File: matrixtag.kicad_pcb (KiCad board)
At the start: 2 copper layers, 57 x 32 mm, 24 parts, among them P1 ISP, Q1 2N7002, Q2 2N7002, Q3 2N7002, Q4 2N7002, Q5 2N7002, Q6 2N7002, Q7 2N7002, Q8 2N7002, SW1 RESET, U1 ATTINY4313-S

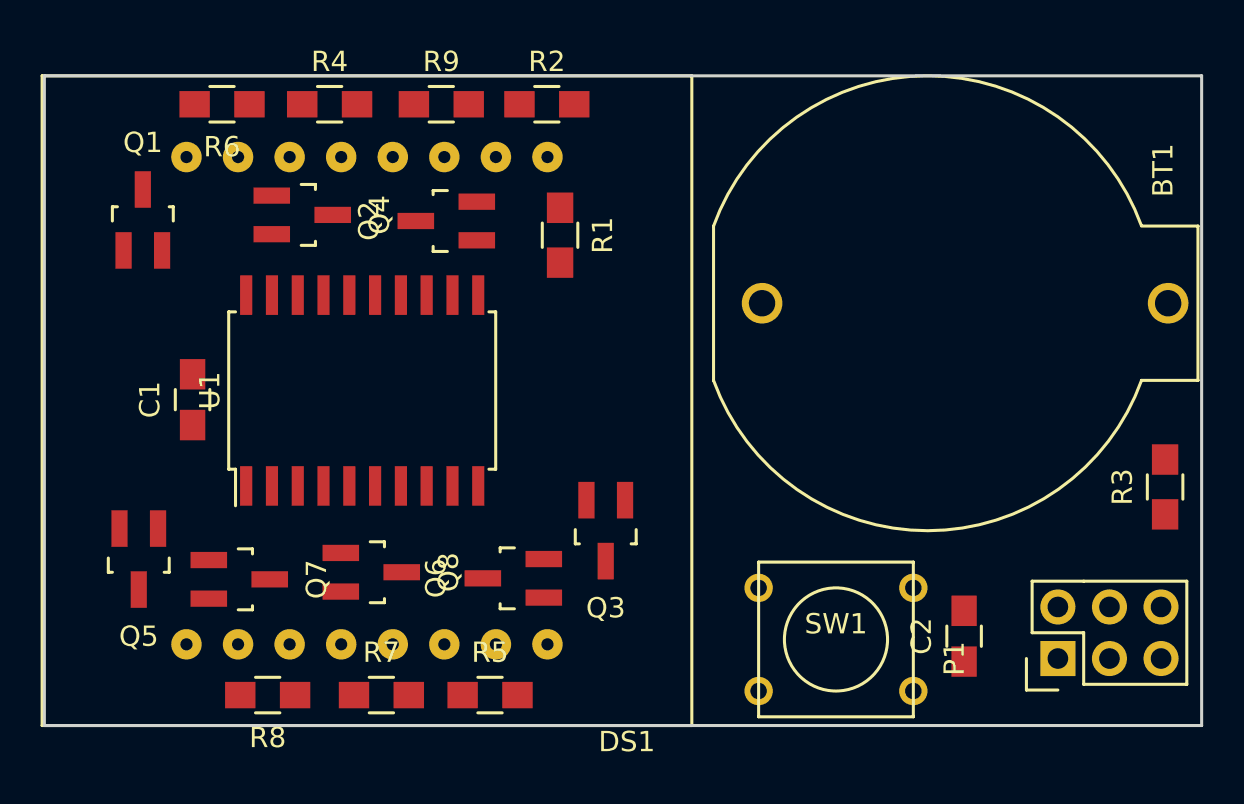
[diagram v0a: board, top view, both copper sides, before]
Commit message: Moved parts to front layer
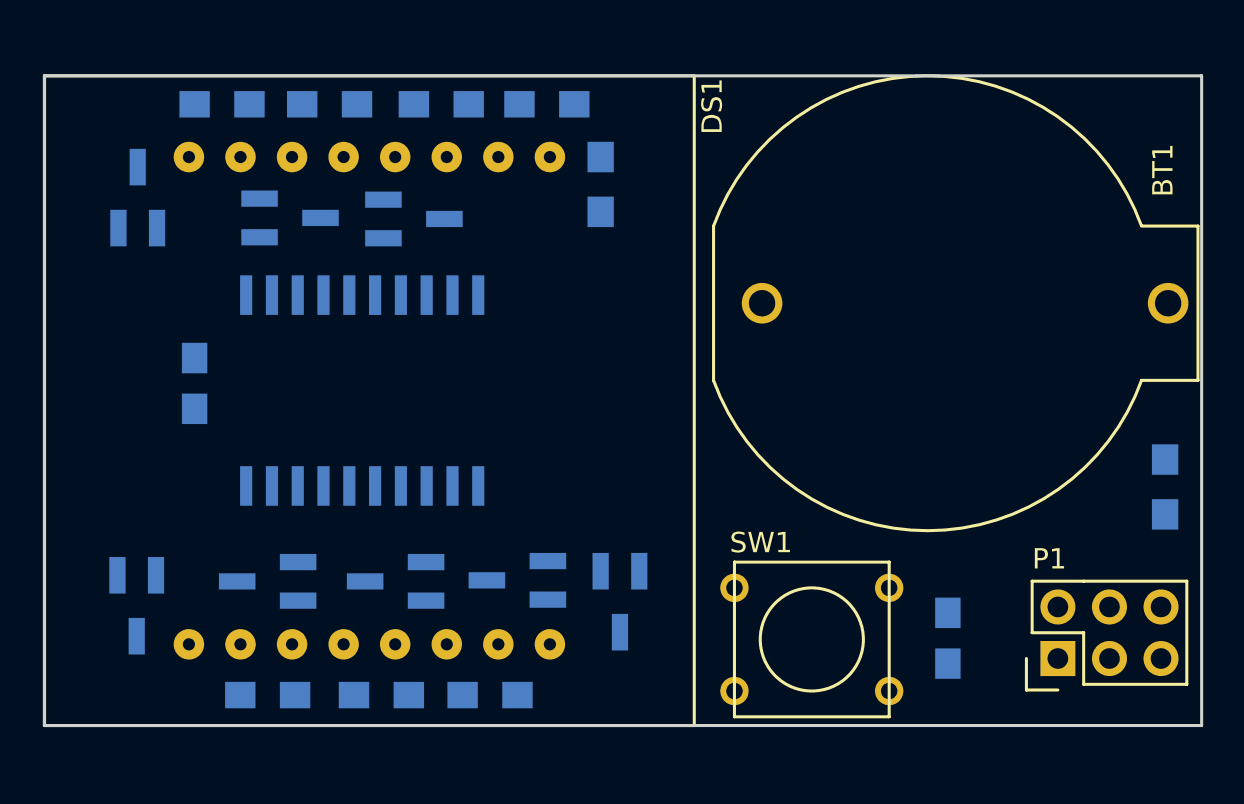
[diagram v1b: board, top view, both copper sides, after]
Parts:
- C1, C2, Q1, Q2, Q3, Q4, Q5, Q6, Q7, Q8, R1, R2, R3, R4, R5, R6, R7, R8, R9, U1: moved to B.Cu
- moved Q3 3.57 mm to (196.3, 112.9), turned to 0 degrees
- moved R1 3.20 mm to (195.4, 92.3)
- moved Q5 2.30 mm to (172.6, 113.1), turned to 0 degrees
- moved Q2 1.60 mm to (186.2, 94.0)
- moved Q7 1.40 mm to (179.0, 111.9)
- moved Q8 1.28 mm to (185.3, 111.9)
- moved SW1 1.19 mm to (205.8, 114.8)
- moved Q1 1.13 mm to (172.6, 93.0), turned to 180 degrees
- moved C2 0.81 mm to (212.5, 114.7), turned to 270 degrees
- moved C1 0.81 mm to (175.4, 102.2), turned to 270 degrees
- moved Q4 0.62 mm to (180.1, 94.0), turned to 90 degrees
- moved Q6 0.22 mm to (191.3, 111.8), turned to 270 degrees
- moved DS1 0.12 mm to (184.0, 103.0)
- turned R3 to 270 degrees
- turned U1 to 270 degrees

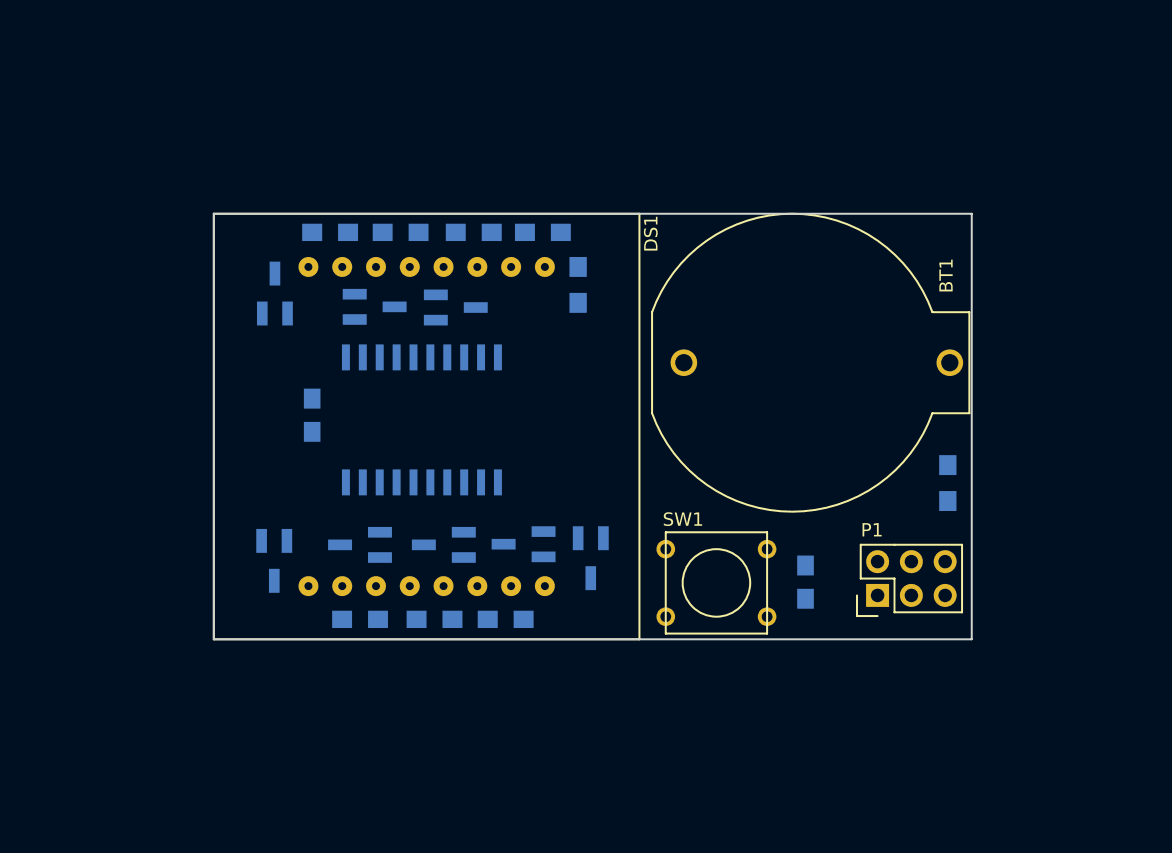
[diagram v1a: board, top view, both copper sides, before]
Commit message: Finished matrix tag schematic and layout
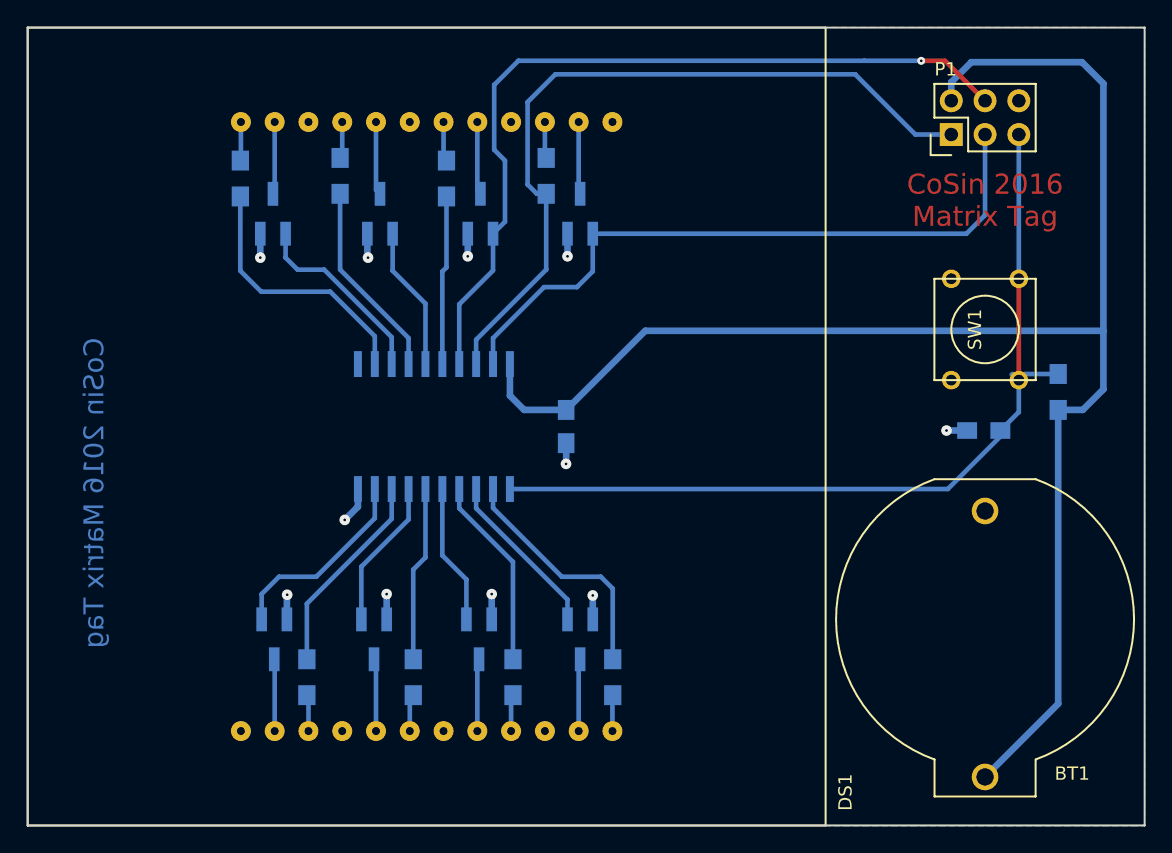
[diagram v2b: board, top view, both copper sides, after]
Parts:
- DS1: value LDM-1088AX -> CSM-88261EG; footprint nametag:LDM-1088 -> nametag:CSM-88261
- moved P1 35.1 mm to (223.5, 81.0)
- moved R7 34.1 mm to (177.5, 84.2), turned to 270 degrees
- moved R8 33.8 mm to (185.5, 84.3), turned to 270 degrees
- moved R2 33.5 mm to (190.5, 121.8), turned to 90 degrees
- moved R4 33.5 mm to (183.0, 121.8), turned to 90 degrees
- moved Q3 30.4 mm to (180.5, 87.0), turned to 180 degrees
- moved R1 29.6 mm to (198.0, 121.8), turned to 90 degrees
- moved SW1 27.8 mm to (226.0, 95.7), turned to 90 degrees
- moved BT1 24.1 mm to (226.0, 117.5), turned to 270 degrees
- moved Q1 23.7 mm to (195.6, 87.0)
- moved C1 19.1 mm to (194.5, 103.0), turned to 90 degrees
- moved C2 17.6 mm to (225.9, 103.3), turned to 180 degrees
- moved R5 15.6 mm to (175.0, 121.8), turned to 90 degrees
- moved Q6 13.3 mm to (180.1, 119.0), turned to 0 degrees
- moved Q8 12.5 mm to (195.6, 119.0), turned to 0 degrees
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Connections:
- DS1 pad 1: Net-(DS1-Pad1) -> (no net)
- DS1 pad 10: Net-(DS1-Pad10) -> (no net)
- DS1 pad 15: Net-(DS1-Pad15) -> (no net)
- DS1 pad 4: Net-(DS1-Pad4) -> (no net)
- DS1 pad 7: Net-(DS1-Pad7) -> (no net)
- P1 pad 1: /COL7 -> /MISO
- P1 pad 2: (no net) -> VCC
- P1 pad 3: /COL8 -> /COL1
- P1 pad 4: /COL6 -> /COL2
- Q1 pad 1: /ROW1 -> /COL1
- Q1 pad 3: Net-(DS1-Pad9) -> Net-(DS1-Pad23)
- Q2 pad 1: /ROW2 -> /COL2
- Q2 pad 3: Net-(DS1-Pad14) -> Net-(DS1-Pad20)
- Q3 pad 1: /ROW3 -> /COL3
- Q3 pad 3: Net-(DS1-Pad8) -> Net-(DS1-Pad17)
- Q4 pad 1: /ROW4 -> /COL4
- Q4 pad 3: Net-(DS1-Pad12) -> Net-(DS1-Pad14)
- Q5 pad 1: /ROW5 -> /COL5
- Q5 pad 3: Net-(DS1-Pad1) -> Net-(DS1-Pad2)
- Q6 pad 1: /ROW6 -> /COL6
- Q6 pad 3: Net-(DS1-Pad7) -> Net-(DS1-Pad5)
- Q7 pad 1: /ROW7 -> /COL7
- Q7 pad 3: Net-(DS1-Pad2) -> Net-(DS1-Pad8)
- Q8 pad 1: /ROW8 -> /COL8
- Q8 pad 3: Net-(DS1-Pad5) -> Net-(DS1-Pad11)
- R1 pad 1: Net-(DS1-Pad16) -> Net-(DS1-Pad12)
- R1 pad 2: /COL8 -> /ROW8
- R2 pad 1: Net-(DS1-Pad15) -> Net-(DS1-Pad9)
- R2 pad 2: /COL7 -> /ROW7
- R4 pad 1: Net-(DS1-Pad11) -> Net-(DS1-Pad6)
- R4 pad 2: /COL6 -> /ROW6
- R5 pad 1: Net-(DS1-Pad6) -> Net-(DS1-Pad3)
- R5 pad 2: /COL5 -> /ROW5
- R6 pad 1: Net-(DS1-Pad10) -> Net-(DS1-Pad13)
- R6 pad 2: /COL4 -> /ROW4
- R7 pad 1: Net-(DS1-Pad4) -> Net-(DS1-Pad16)
- R7 pad 2: /COL3 -> /ROW3
- R8 pad 1: Net-(DS1-Pad3) -> Net-(DS1-Pad19)
- R8 pad 2: /COL2 -> /ROW2
- R9 pad 1: Net-(DS1-Pad13) -> Net-(DS1-Pad22)
- R9 pad 2: /COL1 -> /MISO
- U1 pad 11: /ROW7 -> (no net)
- U1 pad 12: /COL1 -> /ROW4
- U1 pad 13: /COL2 -> /COL4
- U1 pad 14: /COL3 -> /ROW3
- U1 pad 15: /COL4 -> /COL3
- U1 pad 16: /COL5 -> /ROW2
- U1 pad 17: /COL6 -> /COL2
- U1 pad 18: /COL7 -> /MISO
- U1 pad 19: /COL8 -> /COL1
- U1 pad 2: /ROW1 -> /ROW8
- U1 pad 3: /ROW2 -> /COL8
- U1 pad 4: /ROW8 -> /ROW7
- U1 pad 5: (no net) -> /COL7
- U1 pad 6: /ROW3 -> /ROW6
- U1 pad 7: /ROW4 -> /COL6
- U1 pad 9: /ROW6 -> /COL5
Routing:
- net VCC: track 0.00 -> 120.9 mm
- net /~RESET: track 0.00 -> 64.9 mm
- net /COL2: track 0.00 -> 61.7 mm, vias 0 -> 1
- net /MISO: track 0.00 -> 57.5 mm
- net /COL1: track 0.00 -> 50.5 mm
- net GND: track 0.00 -> 20.3 mm, vias 0 -> 11
- net /ROW4: track 0.00 -> 19.8 mm
- net /ROW8: track 0.00 -> 18.2 mm
- net /ROW5: track 0.00 -> 15.4 mm
- net /COL5: track 0.00 -> 15.0 mm
- net /ROW3: track 0.00 -> 14.9 mm
- net /ROW7: track 0.00 -> 14.5 mm
- net /COL4: track 0.00 -> 14.3 mm
- net /ROW6: track 0.00 -> 13.2 mm
- net /ROW2: track 0.00 -> 12.7 mm
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- added copper zone on F.Cu, net GND
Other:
- board size 57 x 32 mm -> 84 x 60 mm
- net class Default: trace_width 0.25 -> 0.35; via_drill 0.4 -> 0.2
- net class Power added: clearance 0.25, trace_width 0.5, via_dia 0.8, via_drill 0.2
- rule via_min_drill: 0.3 -> 0.2
- board text added: "CoSin 2016 Matrix Tag"

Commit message: Some small matrix tag updates
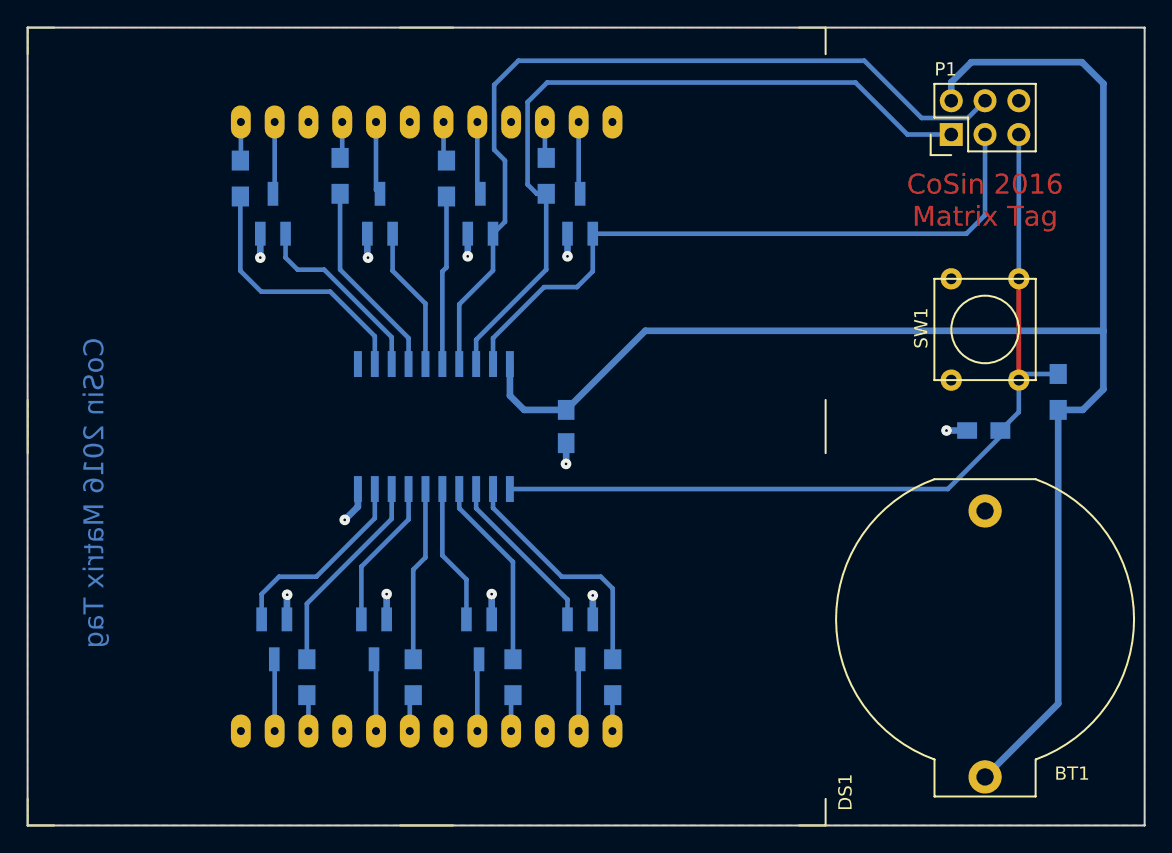
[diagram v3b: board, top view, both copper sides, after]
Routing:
- net /COL2: track 61.7 -> 62.7 mm, vias 1 -> 0
- net /MISO: track 57.5 -> 57.0 mm

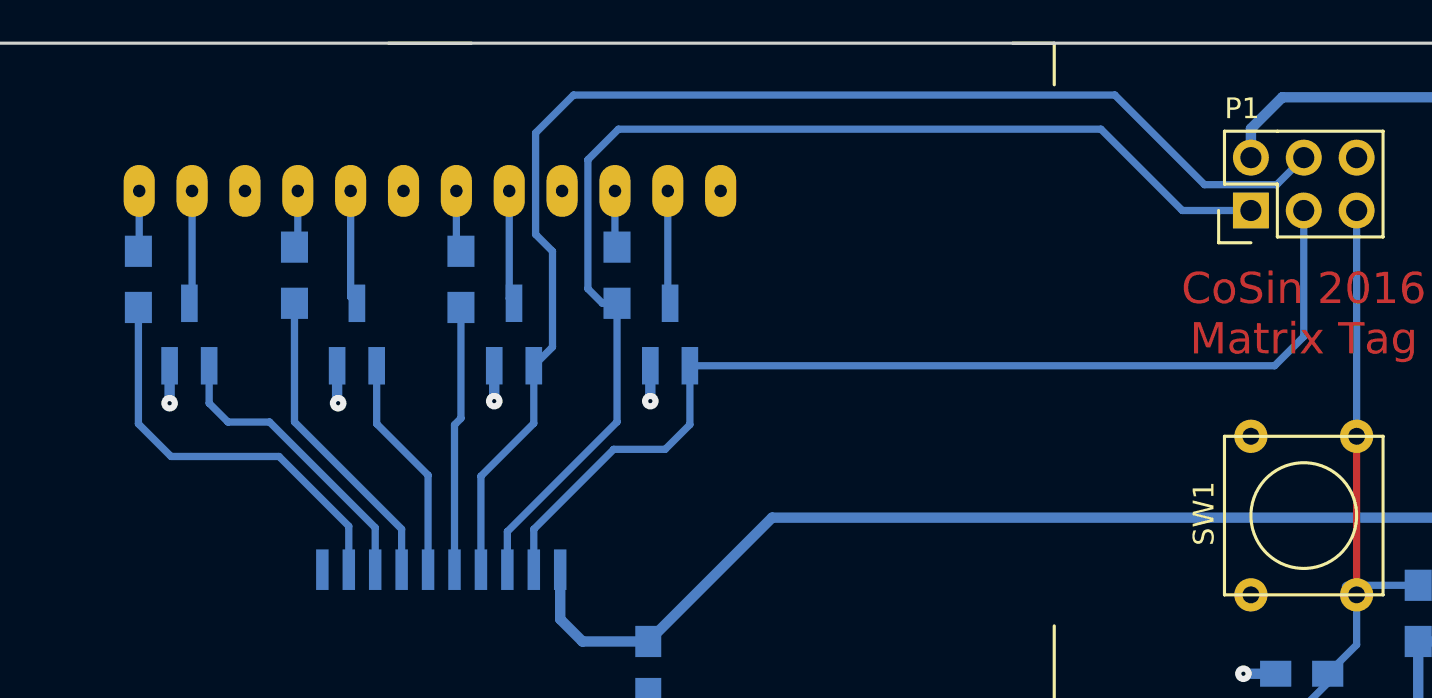
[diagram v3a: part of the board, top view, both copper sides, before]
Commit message: Fixed matrix tag layout with correct panel pinout
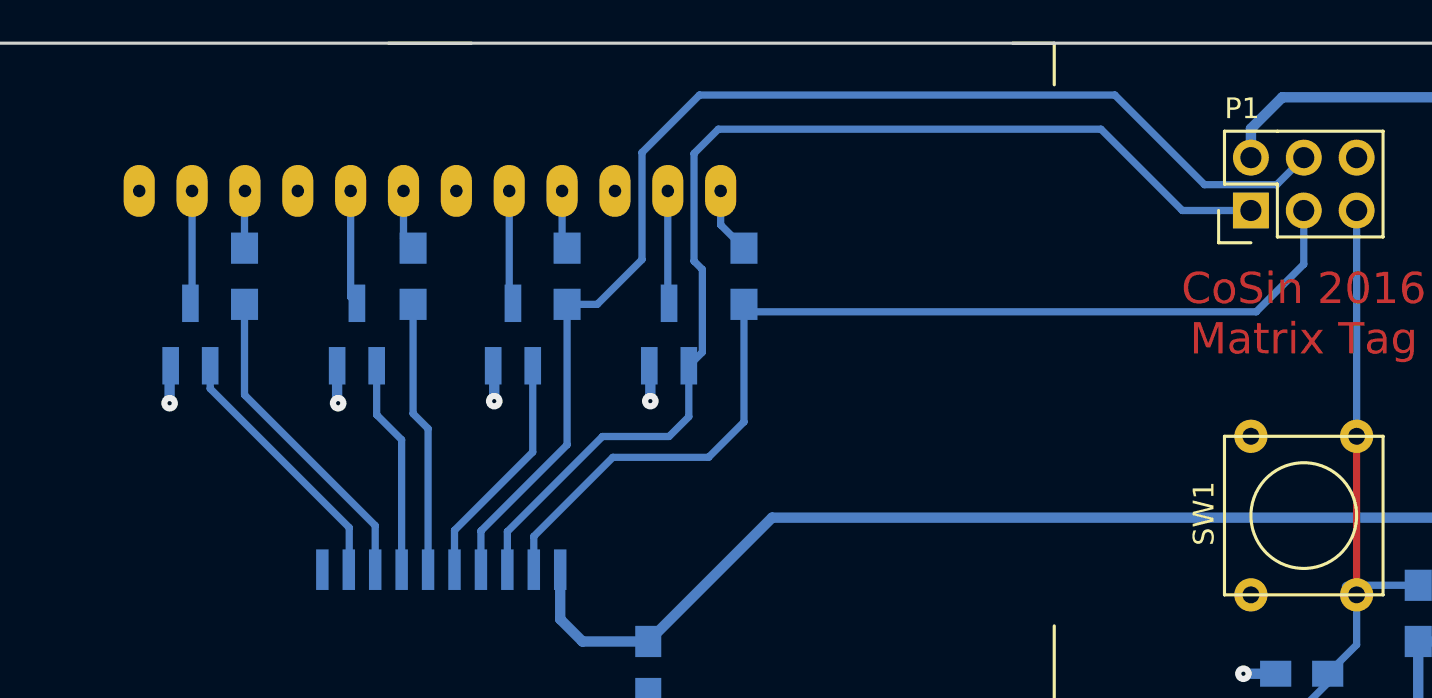
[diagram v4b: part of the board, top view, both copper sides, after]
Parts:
- moved R6 29.1 mm to (199.1, 84.2)
- moved Q1 23.1 mm to (172.5, 87.0)
- moved Q4 23.1 mm to (195.5, 87.0)
- moved R9 17.9 mm to (175.1, 84.2)
- moved R7 13.1 mm to (190.6, 84.2)
- moved Q2 7.55 mm to (180.5, 87.0)
- moved Q3 7.50 mm to (188.0, 87.0)
- moved R8 2.30 mm to (183.2, 84.2)
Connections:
- P1 pad 1: /MISO -> /COL4
- P1 pad 3: /COL1 -> /ROW4
- P1 pad 4: /COL2 -> /MOSI
- R7 pad 2: /ROW3 -> /MOSI
- R9 pad 2: /MISO -> /ROW1
- U1 pad 12: /ROW4 -> /COL1
- U1 pad 13: /COL4 -> /ROW1
- U1 pad 14: /ROW3 -> /COL2
- U1 pad 15: /COL3 -> /ROW2
- U1 pad 16: /ROW2 -> /COL3
- U1 pad 17: /COL2 -> /MOSI
- U1 pad 18: /MISO -> /COL4
- U1 pad 19: /COL1 -> /ROW4
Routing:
- net /MOSI: track 0.00 -> 59.4 mm
- net /MISO: track 57.0 -> 0.00 mm
- net /COL2: track 62.7 -> 10.3 mm
- net /COL4: track 14.3 -> 54.8 mm
- net /COL1: track 50.5 -> 12.6 mm
- net /ROW4: track 19.8 -> 50.2 mm
- net /ROW1: track 0.00 -> 15.4 mm
- net /ROW3: track 14.9 -> 0.00 mm
- net /COL3: track 10.8 -> 11.4 mm
